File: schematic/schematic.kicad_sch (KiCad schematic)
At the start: 5 parts, among them U101 ESP32-DEVKIT-V1, U103 ADXL345, U104 ADXL377

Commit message: general rework
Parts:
- added J102: SD_Card, symbol Connector:SD_Card
- added U106: ~, symbol customs:DEBO_SEN_VIBRA
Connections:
- net 3V3: now also J102.4 (VDD), U106.1 (VCC)
- net GND: now also J102.3 (VSS), J102.6 (VSS), U106.2 (GND)
- net at U104.5 (Z): now also U101.19 (D34)
- net at U104.6 (Y): now also U101.20 (D35)
- net at U104.7 (X): now also U101.22 (D33)
- net at U103.4 (SCL): now also U101.11 (D21)
- net at U103.5 (SDA): now also U101.14 (D22)
- net at U101.10 (D19): now also J102.7 (DAT0)
- net at U101.17 (VP): now also U106.4 (AO)
- net at U101.21 (D32): now also U105.4 (AO)
- net at U101.23 (D25): now also J102.2 (CMD)
- net at U101.8 (D5): now also J102.1 (CD/DAT3)
- net at U101.9 (D18): now also J102.5 (CLK)
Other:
- note added: ""HighG"-Accelerometer"
- note added: ""LowG"-Accelerometer"
- note added: "Temperatursensor"
- note added: "Vibrationssensor"
- note added: "https://raw.githubusercontent.com/RuiSantosdotme/ESP32-Course/master/img/ESP32-DOIT-DEVKIT-V1-Board-Pinout-36-GPIOs.png"
- company: (none) -> FRA-UAS
- title: (none) -> ESP32 Gyroscrope-Logger
- moved on the sheet: U101, U103, U104, U105

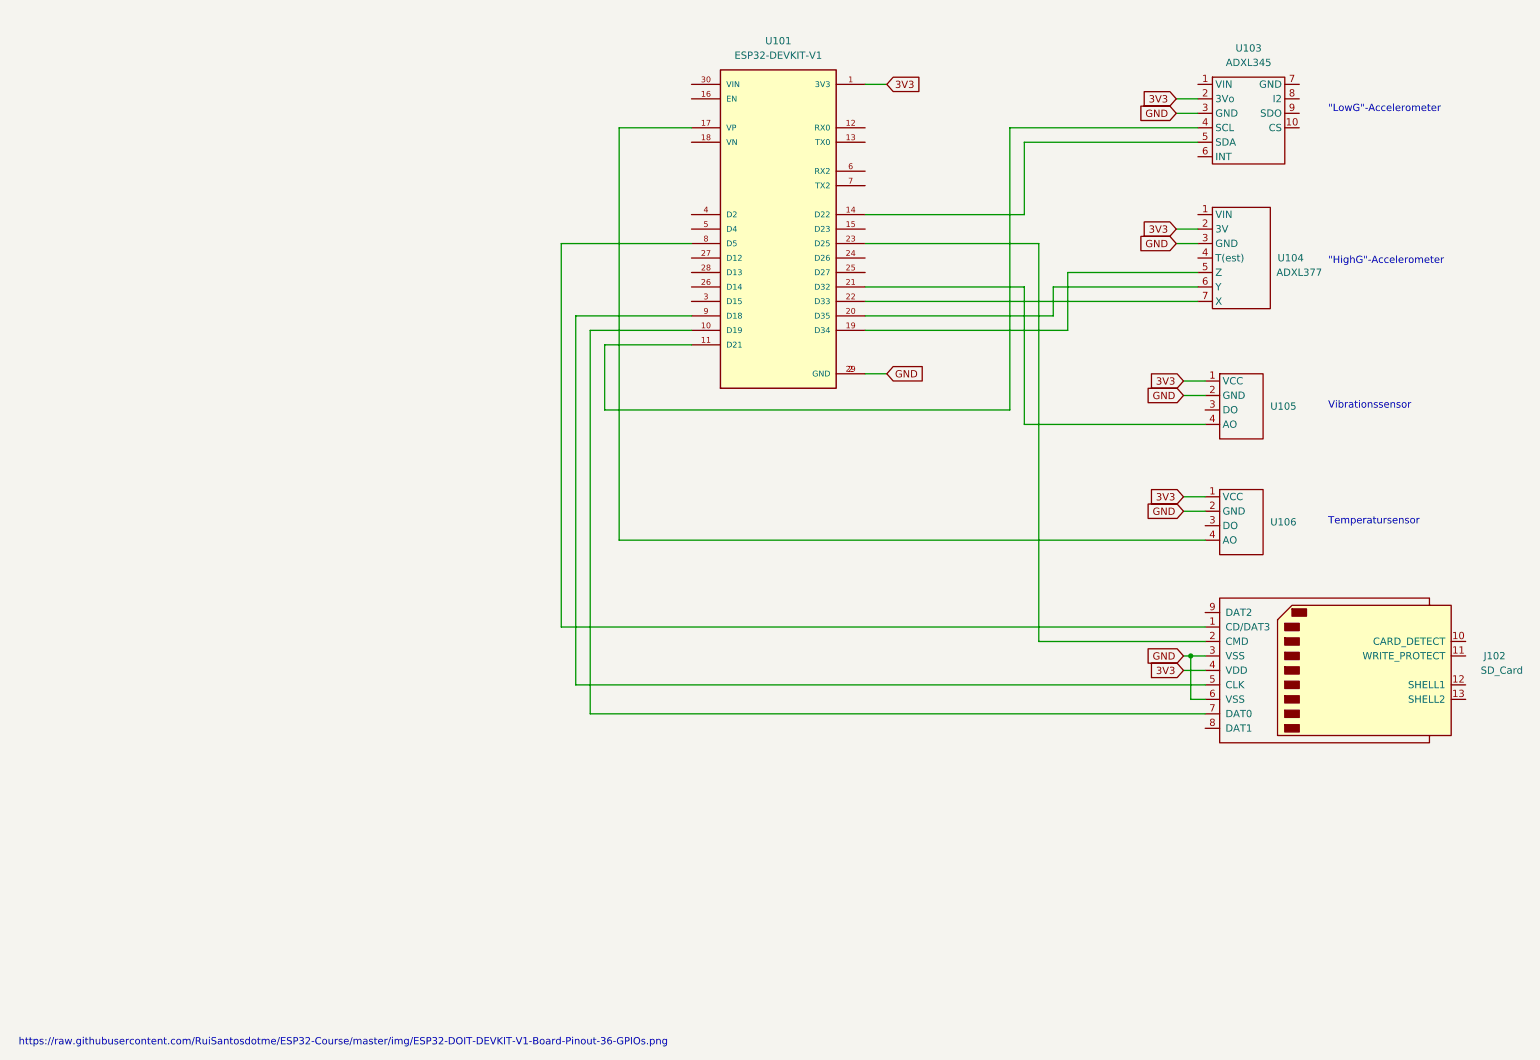
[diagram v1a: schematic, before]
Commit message: delta-inner-outer analysis deployed
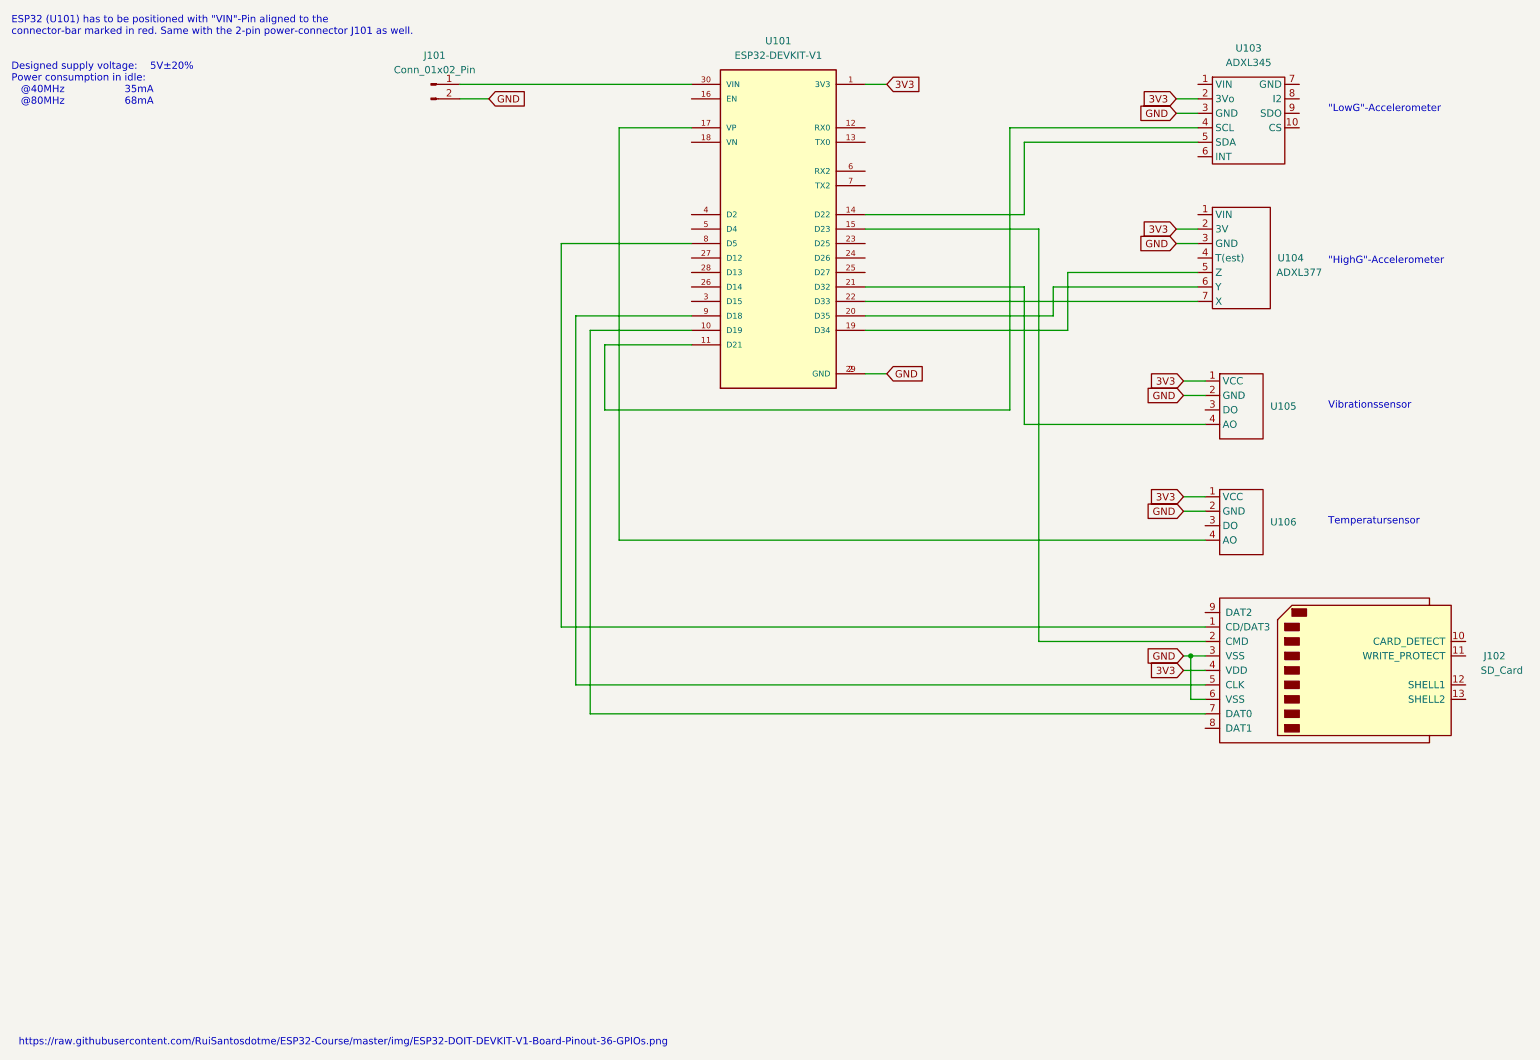
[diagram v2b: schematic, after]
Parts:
- added J101: Conn_01x02_Pin, symbol Connector:Conn_01x02_Pin
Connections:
- net GND: now also J101.2 (Pin_2)
- net at U101.15 (D23): now also J102.2 (CMD)
- net at U101.23 (D25): no longer J102.2 (CMD)
- net at U101.30 (VIN): now also J101.1 (Pin_1)
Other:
- note added: "ESP32 (U101) has to be positioned with "VIN"-Pin aligned to the connector-bar marked in red. Same with the 2-pin power-connector J101 as well. Designed supply voltage: 5V±20% Power consumption in idle: @40MHz 35mA @80MHz 68mA"
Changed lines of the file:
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@@
     (title "ESP32 Gyroscrope-Logger")
     (date "2023-06-16")
-    (rev "Leon Schnieber")
     (company "FRA-UAS")
+    (comment 1 "Leon Schnieber")
   )
   (junction (at 220.98 128.27) (diameter 0) (color 0 0 0 0)
   )
   (wire (pts (xy 223.52 125.73) (xy 194.31 125.73))
-    (stroke (width 0) (type default))
+    (stroke (width 0) (type default) (color 221 133 0 1))
   )
   (wire (pts (xy 133.35 35.56) (xy 120.65 35.56))
@@
   )
   (wire (pts (xy 220.98 128.27) (xy 223.52 128.27))
-    (stroke (width 0) (type default))
+    (stroke (width 0) (type default) (color 0 0 0 1))
+  )
+  (wire (pts (xy 133.35 27.94) (xy 92.71 27.94))
+    (stroke (width 0) (type default) (color 255 0 0 1))
   )
   (wire (pts (xy 218.44 55.88) (xy 222.25 55.88))
-    (stroke (width 0) (type default))
+    (stroke (width 0) (type default) (color 0 0 0 1))
   )
   (wire (pts (xy 189.23 85.09) (xy 118.11 85.09))
-    (stroke (width 0) (type default))
+    (stroke (width 0) (type default) (color 0 0 194 1))
   )
   (wire (pts (xy 163.83 66.04) (xy 222.25 66.04))
-    (stroke (width 0) (type default))
+    (stroke (width 0) (type default) (color 194 0 0 1))
   )
   (wire (pts (xy 118.11 85.09) (xy 118.11 73.66))
-    (stroke (width 0) (type default))
+    (stroke (width 0) (type default) (color 0 0 194 1))
   )
-  (wire (pts (xy 194.31 125.73) (xy 194.31 55.88))
-    (stroke (width 0) (type default))
+  (wire (pts (xy 194.31 53.34) (xy 194.31 125.73))
+    (stroke (width 0) (type default) (color 221 133 0 1))
   )
   (wire (pts (xy 219.71 128.27) (xy 220.98 128.27))
-    (stroke (width 0) (type default))
+    (stroke (width 0) (type default) (color 0 0 0 1))
   )
   (wire (pts (xy 218.44 53.34) (xy 222.25 53.34))
-    (stroke (width 0) (type default))
+    (stroke (width 0) (type default) (color 255 0 0 1))
   )
   (wire (pts (xy 191.77 50.8) (xy 163.83 50.8))
-    (stroke (width 0) (type default))
+    (stroke (width 0) (type default) (color 0 0 194 1))
   )
   (wire (pts (xy 163.83 63.5) (xy 191.77 63.5))
@@
   )
   (wire (pts (xy 218.44 33.02) (xy 222.25 33.02))
-    (stroke (width 0) (type default))
+    (stroke (width 0) (type default) (color 0 0 0 1))
   )
   (wire (pts (xy 219.71 82.55) (xy 223.52 82.55))
-    (stroke (width 0) (type default))
+    (stroke (width 0) (type default) (color 0 0 0 1))
   )
   (wire (pts (xy 220.98 135.89) (xy 220.98 128.27))
-    (stroke (width 0) (type default))
+    (stroke (width 0) (type default) (color 0 0 0 1))
   )
   (wire (pts (xy 110.49 55.88) (xy 110.49 123.19))
-    (stroke (width 0) (type default))
+    (stroke (width 0) (type default) (color 221 133 0 1))
   )
   (wire (pts (xy 113.03 133.35) (xy 113.03 68.58))
-    (stroke (width 0) (type default))
+    (stroke (width 0) (type default) (color 221 133 0 1))
   )
   (wire (pts (xy 219.71 130.81) (xy 223.52 130.81))
-    (stroke (width 0) (type default))
+    (stroke (width 0) (type default) (color 255 0 0 1))
   )
   (wire (pts (xy 223.52 135.89) (xy 220.98 135.89))
-    (stroke (width 0) (type default))
+    (stroke (width 0) (type default) (color 0 0 0 1))
   )
   (wire (pts (xy 113.03 68.58) (xy 133.35 68.58))
-    (stroke (width 0) (type default))
+    (stroke (width 0) (type default) (color 221 133 0 1))
   )
   (wire (pts (xy 199.39 71.12) (xy 163.83 71.12))
-    (stroke (width 0) (type default))
+    (stroke (width 0) (type default) (color 194 0 0 1))
   )
   (wire (pts (xy 218.44 30.48) (xy 222.25 30.48))
-    (stroke (width 0) (type default))
+    (stroke (width 0) (type default) (color 255 0 0 1))
   )
   (wire (pts (xy 163.83 78.74) (xy 167.64 78.74))
-    (stroke (width 0) (type default))
+    (stroke (width 0) (type default) (color 0 0 0 1))
+  )
+  (wire (pts (xy 92.71 30.48) (xy 97.79 30.48))
+    (stroke (width 0) (type default) (color 0 0 0 1))
   )
   (wire (pts (xy 223.52 138.43) (xy 115.57 138.43))
-    (stroke (width 0) (type default))
+    (stroke (width 0) (type default) (color 221 133 0 1))
   )
   (wire (pts (xy 115.57 138.43) (xy 115.57 71.12))
-    (stroke (width 0) (type default))
+    (stroke (width 0) (type default) (color 221 133 0 1))
   )
   (wire (pts (xy 219.71 100.33) (xy 223.52 100.33))
-    (stroke (width 0) (type default))
+    (stroke (width 0) (type default) (color 255 0 0 1))
   )
   (wire (pts (xy 110.49 55.88) (xy 133.35 55.88))
-    (stroke (width 0) (type default))
+    (stroke (width 0) (type default) (color 221 133 0 1))
   )
   (wire (pts (xy 196.85 68.58) (xy 163.83 68.58))
-    (stroke (width 0) (type default))
+    (stroke (width 0) (type default) (color 194 0 0 1))
   )
   (wire (pts (xy 222.25 60.96) (xy 199.39 60.96))
-    (stroke (width 0) (type default))
+    (stroke (width 0) (type default) (color 194 0 0 1))
   )
   (wire (pts (xy 191.77 38.1) (xy 191.77 50.8))
-    (stroke (width 0) (type default))
+    (stroke (width 0) (type default) (color 0 0 194 1))
   )
   (wire (pts (xy 222.25 38.1) (xy 191.77 38.1))
-    (stroke (width 0) (type default))
+    (stroke (width 0) (type default) (color 0 0 194 1))
   )
   (wire (pts (xy 120.65 35.56) (xy 120.65 107.95))
@@
   )
   (wire (pts (xy 189.23 35.56) (xy 189.23 85.09))
-    (stroke (width 0) (type default))
+    (stroke (width 0) (type default) (color 0 0 194 1))
   )
   (wire (pts (xy 115.57 71.12) (xy 133.35 71.12))
-    (stroke (width 0) (type default))
+    (stroke (width 0) (type default) (color 221 133 0 1))
   )
   (wire (pts (xy 120.65 107.95) (xy 223.52 107.95))
@@
   )
   (wire (pts (xy 222.25 35.56) (xy 189.23 35.56))
-    (stroke (width 0) (type default))
+    (stroke (width 0) (type default) (color 0 0 194 1))
   )
   (wire (pts (xy 163.83 27.94) (xy 167.64 27.94))
-    (stroke (width 0) (type default))
+    (stroke (width 0) (type default) (color 255 0 0 1))
   )
   (wire (pts (xy 222.25 63.5) (xy 196.85 63.5))
-    (stroke (width 0) (type default))
+    (stroke (width 0) (type default) (color 194 0 0 1))
   )
   (wire (pts (xy 196.85 63.5) (xy 196.85 68.58))
-    (stroke (width 0) (type default))
+    (stroke (width 0) (type default) (color 194 0 0 1))
   )
   (wire (pts (xy 118.11 73.66) (xy 133.35 73.66))
-    (stroke (width 0) (type default))
+    (stroke (width 0) (type default) (color 0 0 194 1))
   )
-  (wire (pts (xy 194.31 55.88) (xy 163.83 55.88))
-    (stroke (width 0) (type default))
+  (wire (pts (xy 194.31 53.34) (xy 163.83 53.34))
+    (stroke (width 0) (type default) (color 221 133 0 1))
   )
   (wire (pts (xy 219.71 102.87) (xy 223.52 102.87))
-    (stroke (width 0) (type default))
+    (stroke (width 0) (type default) (color 0 0 0 1))
   )
   (wire (pts (xy 199.39 60.96) (xy 199.39 71.12))
-    (stroke (width 0) (type default))
+    (stroke (width 0) (type default) (color 194 0 0 1))
   )
   (wire (pts (xy 191.77 63.5) (xy 191.77 87.63))
@@
   )
   (wire (pts (xy 219.71 80.01) (xy 223.52 80.01))
-    (stroke (width 0) (type default))
+    (stroke (width 0) (type default) (color 255 0 0 1))
   )
   (wire (pts (xy 223.52 133.35) (xy 113.03 133.35))
-    (stroke (width 0) (type default))
+    (stroke (width 0) (type default) (color 221 133 0 1))
   )
   (wire (pts (xy 110.49 123.19) (xy 223.52 123.19))
-    (stroke (width 0) (type default))
+    (stroke (width 0) (type default) (color 221 133 0 1))
   )
   (image (at 69.85 157.48) (scale 1.8817)
@@
     (effects (font (size 1.27 1.27)) (justify left bottom))
   )
+  (text "ESP32 (U101) has to be positioned with \"VIN\"-Pin aligned to the\nconnector-bar marked in red. Same with the 2-pin power-connector J101 as well.\n\n\nDesigned supply voltage:    5V±20%\nPower consumption in idle:  \n   @40MHz                   35mA\n   @80MHz                   68mA"
+    (at 13.97 31.75 0)
+    (effects (font (size 1.27 1.27)) (justify left bottom))
+  )
   (text "\"LowG\"-Accelerometer" (at 245.11 33.02 0)
     (effects (font (size 1.27 1.27)) (justify left bottom))
@@
     )
   )
+  (global_label "GND" (shape input) (at 97.79 30.48 0) (fields_autoplaced)
+    (effects (font (size 1.27 1.27)) (justify left))
+    (property "Intersheetrefs" "${INTERSHEET_REFS}" (at 104.5663 30.48 0)
+      (effects (font (size 1.27 1.27)) (justify left) hide)
+    )
+  )
   (global_label "3V3" (shape input) (at 219.71 100.33 180) (fields_autoplaced)
     (effects (font (size 1.27 1.27)) (justify right))
@@
     )
   )
+  (symbol (lib_id "Connector:Conn_01x02_Pin") (at 87.63 27.94 0) (unit 1)
+    (in_bom yes) (on_board yes) (dnp no) (fields_autoplaced)
+    (property "Reference" "J101" (at 88.265 22.86 0)
+      (effects (font (size 1.27 1.27)))
+    )
+    (property "Value" "Conn_01x02_Pin" (at 88.265 25.4 0)
+      (effects (font (size 1.27 1.27)))
+    )
+    (property "Footprint" "" (at 87.63 27.94 0)
+      (effects (font (size 1.27 1.27)) hide)
+    )
+    (property "Datasheet" "~" (at 87.63 27.94 0)
+      (effects (font (size 1.27 1.27)) hide)
+    )
+    (pin "1")
+    (pin "2")
+    (instances
+      (project "schematic"
+        (path "/ec37ec9d-8c88-43bd-8c86-1349996f53b4"
+          (reference "J101") (unit 1)
+        )
+      )
+    )
+  )
